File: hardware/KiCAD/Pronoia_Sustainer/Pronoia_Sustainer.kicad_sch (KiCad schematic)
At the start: 20 parts, among them J1 XT30PW-M, J2 Screw_Terminal_01x02, J4 Servo0, J5 Servo0, J6 Servo0, J7 Servo0, U1 TPS563201, U2 Teensy4.1, U3 AP2112K-3.3

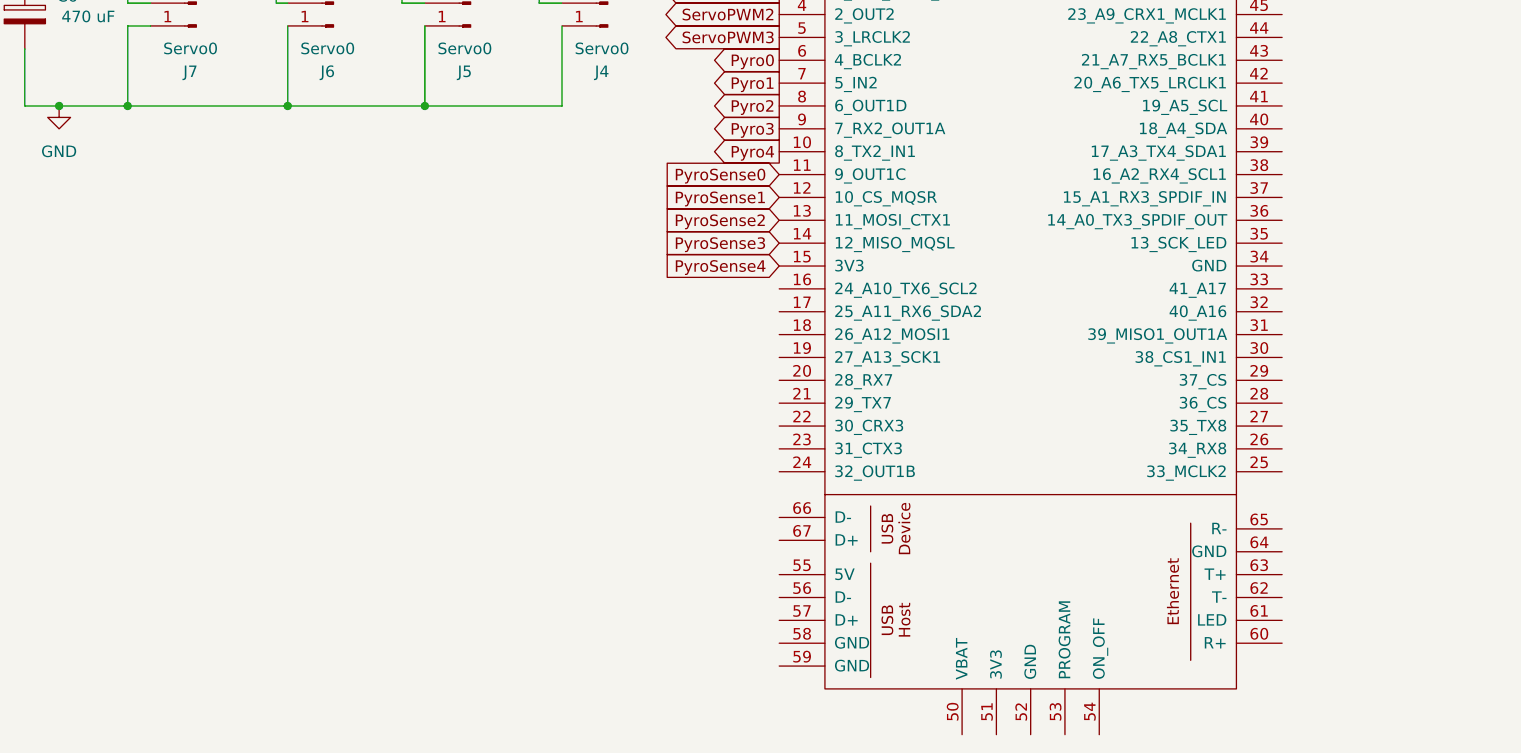
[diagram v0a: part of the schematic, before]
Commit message: Added IMU and connections
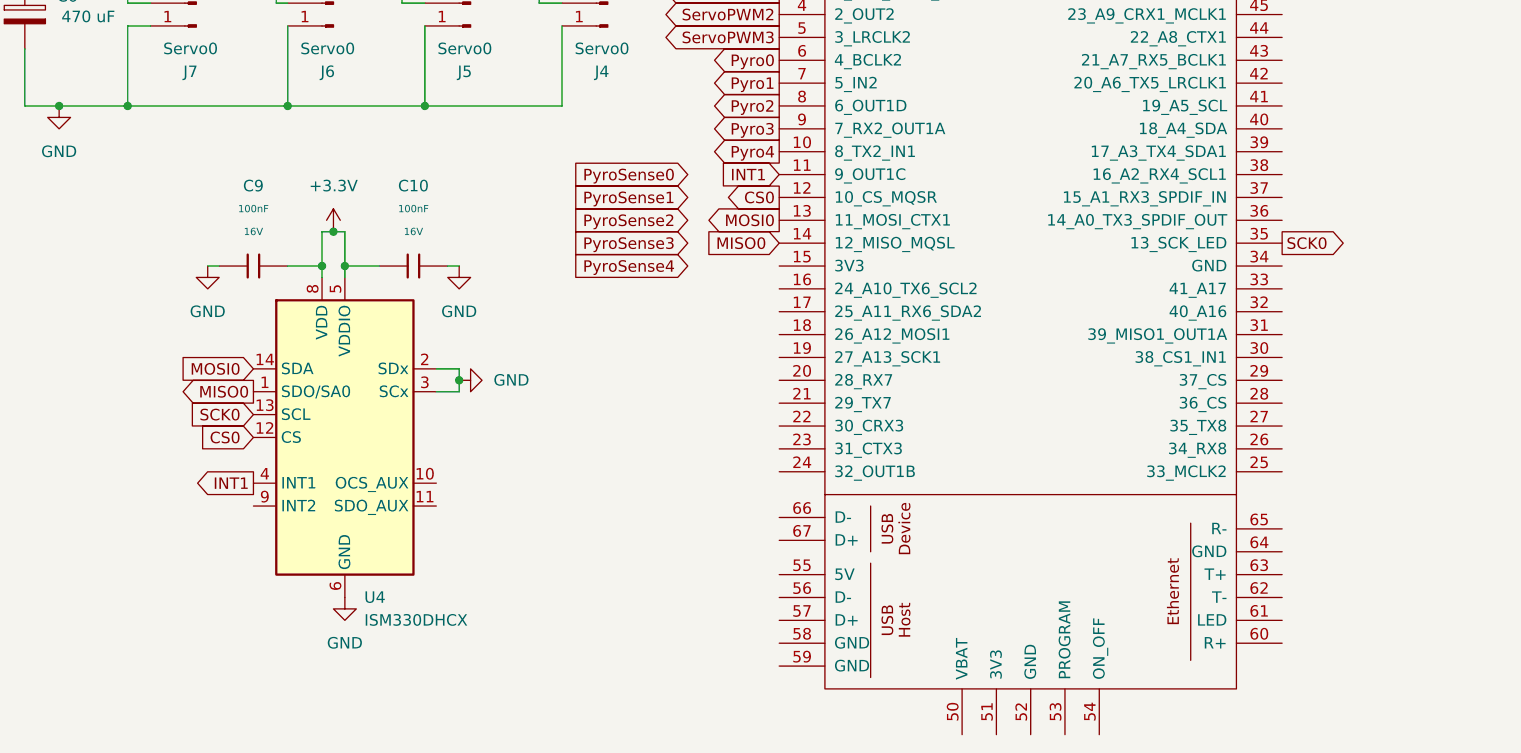
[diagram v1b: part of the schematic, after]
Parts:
- added C10, C9: 100nF, PCM_JLCPCB:C_0402, symbol PCM_JLCPCB-Capacitors:0402,100nF
- added U4: ISM330DHCX, Package_LGA:LGA-14_3x2.5mm_P0.5mm_LayoutBorder3x4y, symbol Sensor_Motion:ISM330DHCX
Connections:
- net +3.3V: now also C10.1, C9.2, U4.5 (VDDIO), U4.8 (VDD)
- net GND: now also C10.2, C9.1, U4.2 (SDx), U4.3 (SCx), U4.6 (GND), U4.7 (GND)
- net PyroSense0: no longer U2.11 (9_OUT1C)
- net PyroSense1: no longer U2.12 (10_CS_MQSR)
- net PyroSense2: no longer U2.13 (11_MOSI_CTX1)
- net PyroSense3: no longer U2.14 (12_MISO_MQSL)
- net PyroSense4: no longer U2.15 (3V3)
- net SCK0: now reaches U2.35 (13_SCK_LED)
- net SCK0: now also U4.13 (SCL)
- new net CS0: U2.12 (10_CS_MQSR), U4.12 (CS)
- new net INT1: U2.11 (9_OUT1C), U4.4 (INT1)
- new net MISO0: U2.14 (12_MISO_MQSL), U4.1 (SDO/SA0)
- new net MOSI0: U2.13 (11_MOSI_CTX1), U4.14 (SDA)

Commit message: Added communication symbols to schematic
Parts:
- added BT1: MS621FE-FL11E, MS621FE-FL11E:BAT_MS621FE-FL11E, symbol MS621FE-FL11E:MS621FE-FL11E
- added J12: 132203, Connector_Coaxial:SMA_Amphenol_132203-12_Horizontal, symbol 132203:132203
- added J13: Conn_01x04_Socket, Connector_PinSocket_2.54mm:PinSocket_1x04_P2.54mm_Vertical, symbol Connector:Conn_01x04_Socket
- added U5: MS5611-01BA, Package_LGA:LGA-8_3x5mm_P1.25mm, symbol Sensor_Pressure:MS5611-01BA
- added U6: H3LIS331DL, H3LIS331DL:QFN300X300X100-16N, symbol H3LIS331DL:H3LIS331DL
- added U7: NEO-M9N, RF_GPS:ublox_NEO, symbol RF_GPS:NEO-M9N
- added U8: RFM95W-915S2, RF_Module:HOPERF_RFM9XW_SMD, symbol RF_Module:RFM95W-915S2
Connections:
- net +5V: no longer C6.1, J4.2 (Pin_2), J5.2 (Pin_2), J6.2 (Pin_2), J7.2 (Pin_2)
- net GND: now also U6.10 (GND), U6.12 (GND), U6.13 (GND), U6.16 (GND), U6.5 (GND)
- net V_batt_Post-Switch: now also C6.1, J4.2 (Pin_2), J5.2 (Pin_2), J6.2 (Pin_2), J7.2 (Pin_2)
- new net: U5.4 (CSB), U5.5 (CSB)
- new net: U7.10 (GND), U7.12 (GND), U7.13 (GND), U7.24 (GND)
- new net VDD: U6.14 (VDD), U6.15 (VDD)
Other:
- moved on the sheet: C7, C8, U3

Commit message: Completed 1st Draft
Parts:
- removed BT1: MS621FE-FL11E, MS621FE-FL11E:BAT_MS621FE-FL11E, symbol MS621FE-FL11E:MS621FE-FL11E
- removed C1, C2: 10uF, PCM_JLCPCB:C_1206, symbol PCM_JLCPCB-Capacitors:1206,10uF
- removed C10, C9: 100nF, PCM_JLCPCB:C_0402, symbol PCM_JLCPCB-Capacitors:0402,100nF
- removed C3, C4: 22uF, PCM_JLCPCB:C_0805, symbol PCM_JLCPCB-Capacitors:0805,22uF
- removed C5: 100nF, PCM_JLCPCB:C_1206, symbol PCM_JLCPCB-Capacitors:1206,100nF
- removed C6: 470 uF, Capacitor_SMD:CP_Elec_8x10, symbol Device:C_Polarized
- removed C7, C8: 1uF, PCM_JLCPCB:C_0603, symbol PCM_JLCPCB-Capacitors:0603,1uF
- removed J1: XT30PW-M, XT30PW-M:AMASS_XT30PW-M, symbol XT30PW-M:XT30PW-M
- removed J12: 132203, Connector_Coaxial:SMA_Amphenol_132203-12_Horizontal, symbol 132203:132203
- removed J13: Conn_01x04_Socket, Connector_PinSocket_2.54mm:PinSocket_1x04_P2.54mm_Vertical, symbol Connector:Conn_01x04_Socket
- removed J2: Screw_Terminal_01x02, TerminalBlock_Phoenix:TerminalBlock_Phoenix_MKDS-1,5-2-5.08_1x02_P5.08mm_Horizontal, symbol Connector:Screw_Terminal_01x02
- removed J4, J5, J6, J7: Servo0, Connector_PinHeader_2.54mm:PinHeader_1x03_P2.54mm_Vertical, symbol Connector:Conn_01x03_Pin
- removed L1: 3.3uH, Inductor_SMD:L_Bourns-SRN8040_8x8.15mm, symbol Device:L
- removed R1: 49.9kΩ, PCM_JLCPCB:R_0805, symbol PCM_JLCPCB-Resistors:0805,49.9kΩ
- removed R2: 9.1kΩ, PCM_JLCPCB:R_0805, symbol PCM_JLCPCB-Resistors:0805,9.1kΩ
- removed U1: TPS563201, Package_TO_SOT_SMD:SOT-23-6, symbol Regulator_Switching:TPS563201
- removed U2: Teensy4.1, teensy.pretty-master:Teensy41, symbol teensy:Teensy4.1
- removed U3: AP2112K-3.3, Package_TO_SOT_SMD:SOT-23-5, symbol Regulator_Linear:AP2112K-3.3
- removed U4: ISM330DHCX, Package_LGA:LGA-14_3x2.5mm_P0.5mm_LayoutBorder3x4y, symbol Sensor_Motion:ISM330DHCX
- removed U5: MS5611-01BA, Package_LGA:LGA-8_3x5mm_P1.25mm, symbol Sensor_Pressure:MS5611-01BA
- removed U6: H3LIS331DL, H3LIS331DL:QFN300X300X100-16N, symbol H3LIS331DL:H3LIS331DL
- removed U7: NEO-M9N, RF_GPS:ublox_NEO, symbol RF_GPS:NEO-M9N
- removed U8: RFM95W-915S2, RF_Module:HOPERF_RFM9XW_SMD, symbol RF_Module:RFM95W-915S2
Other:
- sheet PyroChannels renamed High-Power Actuators
- added sheet Communications & Navigation (RF.kicad_sch)
- added sheet Flight Computer (MCU.kicad_sch)
- added sheet GNC Sensors (Sensors.kicad_sch)
- added sheet Power Management (Power.kicad_sch)
- sheet High-Power Actuators: file PyroChannels.kicad_sch -> Actuators.kicad_sch
- sheet High-Power Actuators ports: added Pyro0, Pyro1, Pyro2, Pyro3, Pyro4, PyroChannelPower, PyroSense0, PyroSense1, PyroSense2, PyroSense3, PyroSense4, ServoPWM0, ServoPWM1, ServoPWM2, ServoPWM3, ServoPower; removed none

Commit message: Completed 1st draft of Schematic
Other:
- sheet Flight Computer ports: added none; removed Pyro4, PyroSense4
- sheet High-Power Actuators ports: added none; removed Pyro4, PyroSense4
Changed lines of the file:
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@@
-	(wire
-		(pts
-			(xy 114.3 91.44) (xy 123.19 91.44)
-		)
-		(stroke
-			(width 0)
-			(type default)
-		)
-	)
 	(wire
 		(pts
@@
 		(pts
 			(xy 151.13 71.12) (xy 156.21 71.12)
-		)
-		(stroke
-			(width 0)
-			(type default)
-		)
-	)
-	(wire
-		(pts
-			(xy 114.3 105.41) (xy 123.19 105.41)
 		)
 		(stroke
@@
 	(sheet
 		(at 123.19 53.34)
-		(size 27.94 81.28)
+		(size 27.94 72.39)
 		(exclude_from_sim no)
 		(in_bom yes)
@@
 		)
 		(property "Sheetfile" "MCU.kicad_sch"
-			(at 123.19 135.2046 0)
+			(at 123.19 126.3146 0)
 			(effects
 				(font
@@
 			)
 		)
-		(pin "Pyro4" output
-			(at 123.19 91.44 180)
-			(effects
-				(font
-					(size 1.27 1.27)
-				)
-				(justify left)
-			)
-		)
 		(pin "PyroSense0" input
 			(at 123.19 95.25 180)
@@
 		(pin "PyroSense3" input
 			(at 123.19 102.87 180)
-			(effects
-				(font
-					(size 1.27 1.27)
-				)
-				(justify left)
-			)
-		)
-		(pin "PyroSense4" input
-			(at 123.19 105.41 180)
 			(effects
 				(font
@@
 	(sheet
 		(at 156.21 87.63)
-		(size 39.37 46.99)
+		(size 39.37 38.1)
 		(exclude_from_sim no)
 		(in_bom yes)
@@
 		)
 		(property "Sheetfile" "RF.kicad_sch"
-			(at 156.21 135.2046 0)
+			(at 156.21 126.3146 0)
 			(effects
 				(font
@@
 			)
 		)
-		(pin "Pyro4" input
-			(at 114.3 91.44 0)
-			(effects
-				(font
-					(size 1.27 1.27)
-				)
-				(justify right)
-			)
-		)
 		(pin "PyroSense0" output
 			(at 114.3 95.25 0)
@@
 			(effects
 				(font
-					(size 1.27 1.27)
-				)
-				(justify right)
-			)
-		)
-		(pin "PyroSense4" output
-			(at 114.3 105.41 0)
-			(effects
-				(font

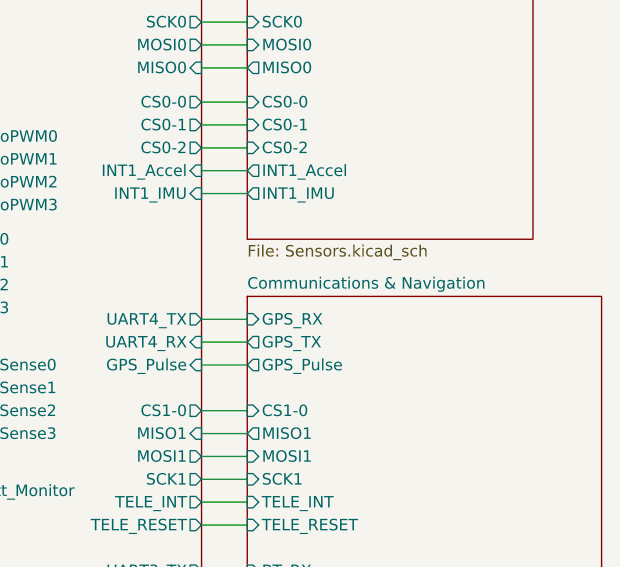
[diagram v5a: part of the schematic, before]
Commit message: Last commit for KiCAD schematic w/ GPS, Telem, and Bluetooth
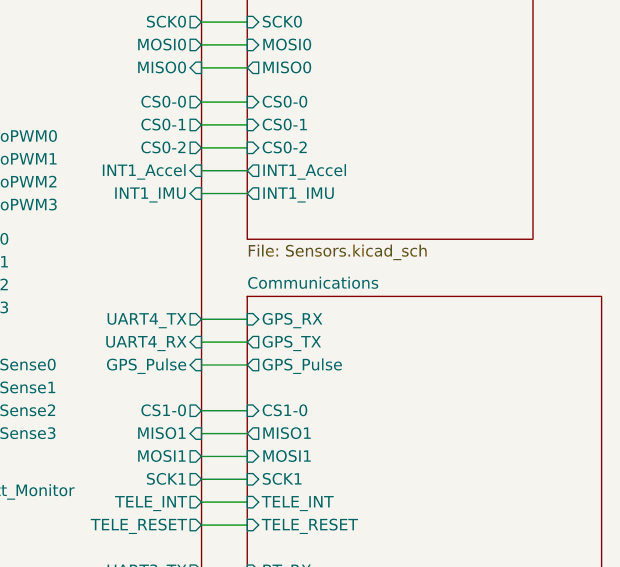
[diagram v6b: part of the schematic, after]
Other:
- sheet Communications & Navigation renamed Communications
- title: Pronoia Sustainer -> Pronoia Sustainer Root
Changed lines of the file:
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@@
 	(paper "A4")
 	(title_block
-		(title "Pronoia Sustainer")
+		(title "Pronoia Sustainer Root")
 		(date "2026-01-22")
 		(rev "1.0")
@@
 			(color 0 0 0 0.0000)
 		)
-		(property "Sheetname" "Communications & Navigation"
+		(property "Sheetname" "Communications"
 			(at 156.21 86.9184 0)
 			(effects

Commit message: Finalized v2.0 of Pronoia Schematic
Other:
- sheet Communications ports: added GX-12-4_Detect, GX-12-4_RX, GX-12-4_TX; removed BT_RX, BT_TX, CS1-0, GPS_Pulse, GPS_RX, GPS_TX, MISO1, MOSI1, SCK1, TELE_INT, TELE_RESET
- sheet Flight Computer ports: added GX-12-4_Detect, RecoveryBuzzPower, UART1_RX, UART1_TX; removed CS0-2, GPS_Pulse, TELE_INT, TELE_RESET, UART3_RX, UART3_TX, UART4_RX, UART4_TX
- sheet GNC Sensors ports: added CS1-0, MISO1, MOSI1, SCK1; removed CS0-2
- sheet Power Management ports: added +8.4V_ARMED, +8.4V_LOGIC; removed Vbatt_Post-Switch

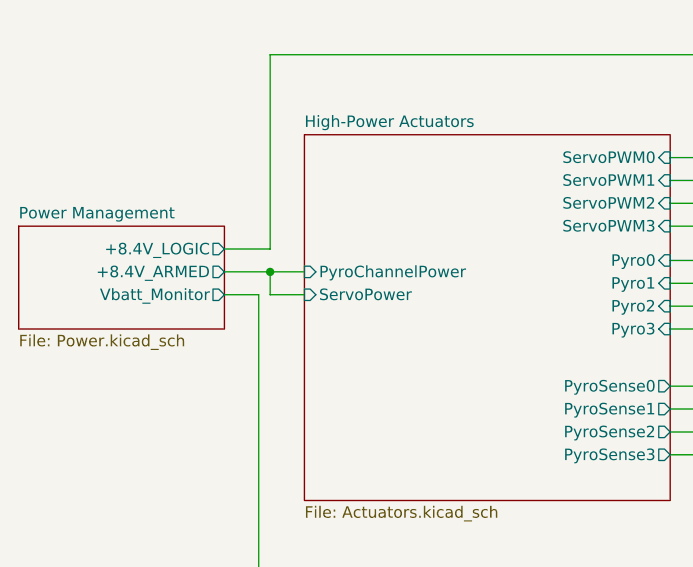
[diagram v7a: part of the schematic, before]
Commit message: Finished PCB layout
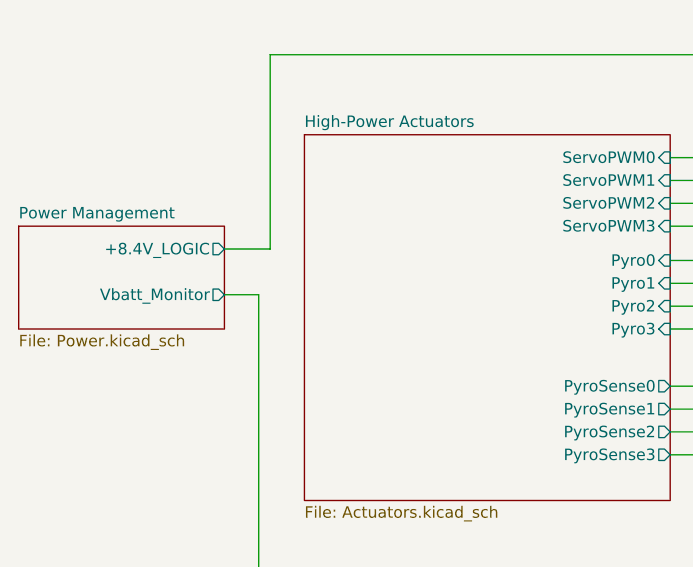
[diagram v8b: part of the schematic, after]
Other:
- sheet High-Power Actuators ports: added none; removed PyroChannelPower, ServoPower
- sheet Power Management ports: added none; removed +8.4V_ARMED
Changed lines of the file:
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@@
 		(comment 1 "Prometheus Rocket Project")
 	)
-	(junction
-		(at 69.85 82.55)
-		(diameter 0)
-		(color 0 0 0 0)
-	)
 	(wire
 		(pts
@@
 	(wire
 		(pts
-			(xy 73.66 85.09) (xy 69.85 85.09)
-		)
-		(stroke
-			(width 0)
-			(type default)
-		)
-	)
-	(wire
-		(pts
 			(xy 153.67 72.39) (xy 165.1 72.39)
 		)
@@
 	(wire
 		(pts
-			(xy 64.77 82.55) (xy 69.85 82.55)
-		)
-		(stroke
-			(width 0)
-			(type default)
-		)
-	)
-	(wire
-		(pts
 			(xy 68.58 115.57) (xy 121.92 115.57)
 		)
@@
 	(wire
 		(pts
-			(xy 69.85 82.55) (xy 69.85 85.09)
-		)
-		(stroke
-			(width 0)
-			(type default)
-		)
-	)
-	(wire
-		(pts
 			(xy 114.3 81.28) (xy 121.92 81.28)
 		)
@@
 		(pts
 			(xy 153.67 69.85) (xy 165.1 69.85)
-		)
-		(stroke
-			(width 0)
-			(type default)
-		)
-	)
-	(wire
-		(pts
-			(xy 69.85 82.55) (xy 73.66 82.55)
 		)
 		(stroke
@@
 			)
 		)
-		(pin "ServoPower" input
-			(at 73.66 85.09 180)
-			(effects
-				(font
-					(size 1.27 1.27)
-				)
-				(justify left)
-			)
-		)
 		(pin "ServoPWM0" input
 			(at 114.3 69.85 0)
@@
 				)
 				(justify right)
-			)
-		)
-		(pin "PyroChannelPower" input
-			(at 73.66 82.55 180)
-			(effects
-				(font
-					(size 1.27 1.27)
-				)
-				(justify left)
 			)
 		)
@@
 			(effects
 				(font
-					(size 1.27 1.27)
-				)
-				(justify right)
-			)
-		)
-		(pin "+8.4V_ARMED" output
-			(at 64.77 82.55 0)
-			(effects
-				(font
